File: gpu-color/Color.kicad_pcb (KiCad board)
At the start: 2 copper layers, 160 x 100 mm, 75 parts, among them J1 C96ABC, J2 Conn_01x26_Male, J3 VGA, J4 I2C, SW1 SW_Coded_SH-7050, U1 74LS161, U10 74LS161, U11 74LS161, U12 74LS161, U13 74LS161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

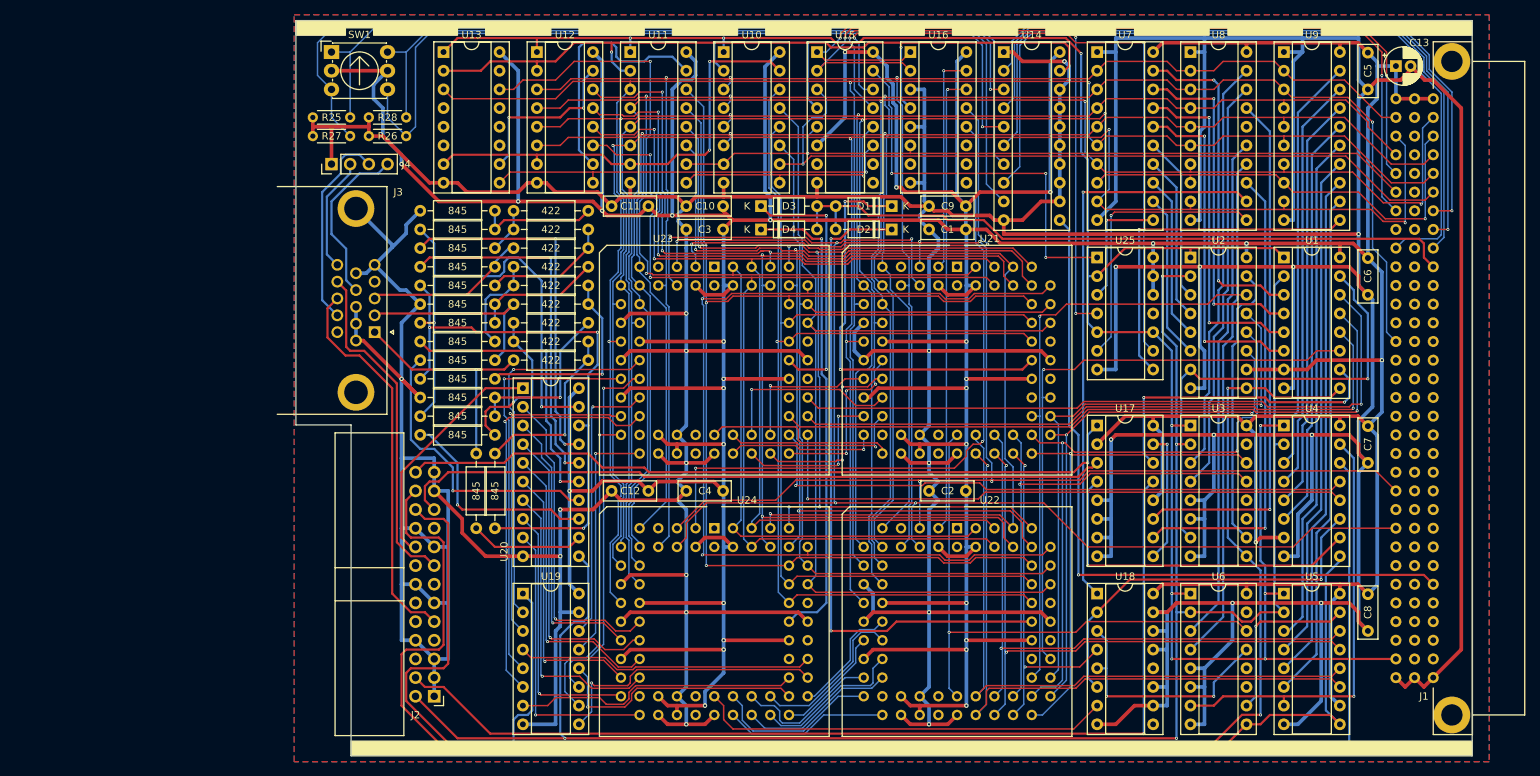
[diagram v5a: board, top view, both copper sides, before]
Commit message: GPU color: add connector for internal screen; add text and logo
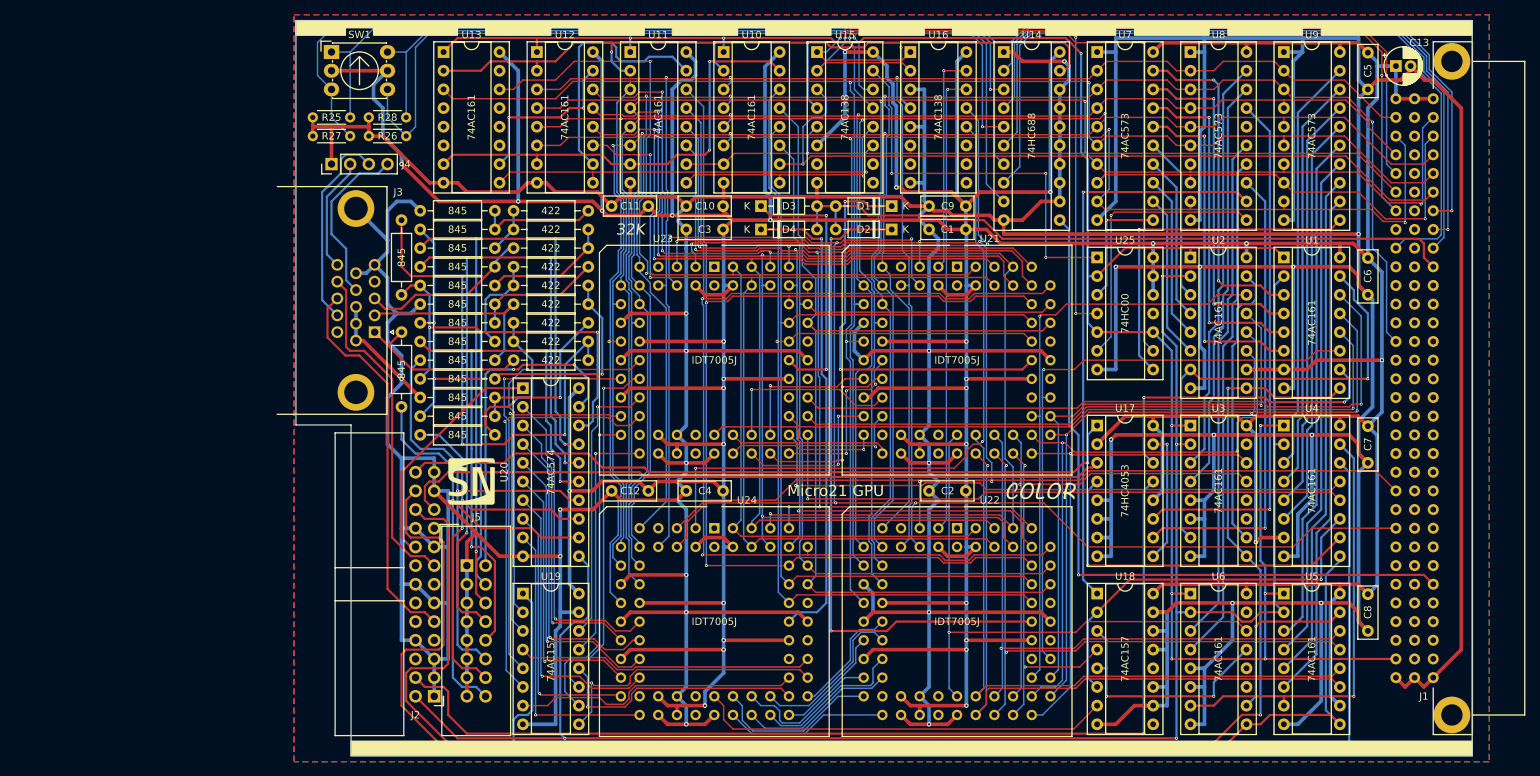
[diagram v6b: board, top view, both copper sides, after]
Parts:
- added G***: LOGO, common:color, F.Cu at (151.4, 114.0)
- added G***: LOGO, common:logo, F.Cu at (73.9, 112.7)
- added J5: Conn_02x08_Odd_Even, Connector_IDC:IDC-Header_2x08_P2.54mm_Vertical, F.Cu at (73.3, 124.1)
- U1, U10, U11, U12, U13, U2, U3, U4, U5, U6: value 74LS161 -> 74AC161
- U15, U16: value 74LS138 -> 74AC138
- U7, U8, U9: value 74LS573 -> 74AC573
- moved R22 34.2 mm to (64.4, 87.3)
- moved R24 19.4 mm to (64.4, 102.5)
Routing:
- net /B1: track 48.9 -> 101.7 mm, vias 2 -> 4
- net /R1: track 15.5 -> 66.3 mm, vias 0 -> 1
- net /B0: track 49.3 -> 99.4 mm, vias 2 -> 4
- net Net-(R21-Pad2): track 24.6 -> 69.0 mm, vias 1 -> 3
- net /G0: track 38.8 -> 80.7 mm, vias 2 -> 4
- net /R0: track 29.7 -> 57.3 mm, vias 1 -> 2
- net /G1: track 39.5 -> 65.4 mm
- net GND: track 1390.7 -> 1414.9 mm
- net /I0: track 68.8 -> 81.5 mm, vias 2 -> 5
- net /I1: track 77.7 -> 89.5 mm
- net /R: track 33.0 -> 24.1 mm, vias 1 -> 0
- net ODDCOL: track 137.0 -> 138.9 mm
- net /B: track 22.1 -> 23.3 mm
- net /Pattern Table/Q0: track 51.7 -> 51.0 mm
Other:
- board text added: "32K"
- board text added: "Micro21 GPU"
